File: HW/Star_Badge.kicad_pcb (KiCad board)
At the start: 2 copper layers, 180 x 171.6 mm, 55 parts, among them J1 AVR-ISP-6, J2 10118194-0001LF, Q1 Q_NMOS_DGS, Q2 Q_PMOS_DGS, U1 ATTINY861-15XD, U2 TPS613221ADBVT, U3 AP7363-33D-13, X1 Badgelife_sao_connector_v169b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, X2 Badgelife_sao_connector_v169b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, X3 Badgelife_sao_connector_v169b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

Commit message: Star 4 - net routing
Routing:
- net /EN_RGB2: track 0.00 -> 44.4 mm
- net Net-(BT1-Pad1): track 46.0 -> 48.3 mm
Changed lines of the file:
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@@
     (thickness 1.6)
     (drawings 611)
-    (tracks 85)
+    (tracks 120)
     (zones 0)
     (modules 55)
@@
   (gr_line (start 100.038258 14.223787) (end 100.038258 14.223787) (layer Edge.Cuts) (width 0.1))
   (segment (start 99.6 155.5) (end 98.95 155.5) (width 0.4572) (layer B.Cu) (net 1))
-  (segment (start 72.85 116.475) (end 66.6 124.1822) (width 0.4572) (layer B.Cu) (net 2))
   (segment (start 79.05 148.5) (end 79.2 148.65) (width 0.4572) (layer B.Cu) (net 2))
-  (segment (start 66.6 124.1822) (end 66.6 141.85) (width 0.4572) (layer B.Cu) (net 2))
-  (segment (start 66.6 141.85) (end 73.25 148.5) (width 0.4572) (layer B.Cu) (net 2))
   (segment (start 73.25 148.5) (end 79.05 148.5) (width 0.4572) (layer B.Cu) (net 2))
   (segment (start 73.2 148.55) (end 73.2 151.5) (width 0.508) (layer B.Cu) (net 2))
   (segment (start 73.25 148.5) (end 73.2 148.55) (width 0.508) (layer B.Cu) (net 2))
+  (segment (start 71.5 148.5) (end 73.25 148.5) (width 0.4572) (layer B.Cu) (net 2))
+  (segment (start 65.5 142.5) (end 71.5 148.5) (width 0.4572) (layer B.Cu) (net 2))
+  (segment (start 72.85 116.475) (end 65.5 123.825) (width 0.4572) (layer B.Cu) (net 2))
+  (segment (start 65.5 123.825) (end 65.5 142.5) (width 0.4572) (layer B.Cu) (net 2))
   (segment (start 107.4 156.45) (end 110.625 153.225) (width 0.4572) (layer B.Cu) (net 3))
   (segment (start 101.55 156) (end 102 156.45) (width 0.4572) (layer B.Cu) (net 3))
@@
   (segment (start 85.7 148.7) (end 85.7 145.6) (width 0.508) (layer B.Cu) (net 5))
   (segment (start 89 150.775) (end 89 146.625) (width 0.508) (layer B.Cu) (net 5))
+  (segment (start 80.6 128.7) (end 80.583073 128.747516) (width 0.2032) (layer B.Cu) (net 11))
+  (segment (start 77.6 125.5) (end 79.5 128.8) (width 0.2032) (layer B.Cu) (net 11))
+  (segment (start 77.3 125.3) (end 77.6 125.5) (width 0.2032) (layer B.Cu) (net 11))
+  (segment (start 73 131.4) (end 73.4 131.3) (width 0.2032) (layer B.Cu) (net 11))
+  (segment (start 72.4 131.5) (end 73 131.4) (width 0.2032) (layer B.Cu) (net 11))
+  (segment (start 76.7 125.5) (end 77 125.3) (width 0.2032) (layer B.Cu) (net 11))
+  (segment (start 73.4 131.3) (end 73.6 131.2) (width 0.2032) (layer B.Cu) (net 11))
+  (segment (start 71.518794 130.675879) (end 72.206625 131.36371) (width 0.2032) (layer B.Cu) (net 11))
+  (segment (start 79.5 128.8) (end 80.1 129.8) (width 0.2032) (layer B.Cu) (net 11))
+  (segment (start 72.206625 131.36371) (end 72.4 131.5) (width 0.2032) (layer B.Cu) (net 11))
+  (segment (start 80.1 129.8) (end 80.6 128.7) (width 0.2032) (layer B.Cu) (net 11))
+  (segment (start 76.3 126.1) (end 76.7 125.5) (width 0.2032) (layer B.Cu) (net 11))
+  (segment (start 73.6 131.2) (end 74.6 129.5) (width 0.2032) (layer B.Cu) (net 11))
+  (segment (start 74.6 129.5) (end 75.2 128.2) (width 0.2032) (layer B.Cu) (net 11))
+  (segment (start 75.2 128.2) (end 76.3 126.1) (width 0.2032) (layer B.Cu) (net 11))
+  (segment (start 77 125.3) (end 77.3 125.3) (width 0.2032) (layer B.Cu) (net 11))
+  (segment (start 80.377778 130.7) (end 80.1 129.8) (width 0.2032) (layer B.Cu) (net 11))
+  (segment (start 80.8 131.2) (end 80.377778 130.7) (width 0.2032) (layer B.Cu) (net 11))
+  (segment (start 83.7 131.8) (end 80.8 131.2) (width 0.2032) (layer B.Cu) (net 11))
+  (segment (start 87 132.3) (end 86.4 132.2) (width 0.2032) (layer B.Cu) (net 11))
+  (segment (start 87.5 133.1) (end 87.4 132.6) (width 0.2032) (layer B.Cu) (net 11))
+  (segment (start 81.1 144) (end 82.6 144.8) (width 0.2032) (layer B.Cu) (net 11))
+  (segment (start 86.4 132.2) (end 83.7 131.8) (width 0.2032) (layer B.Cu) (net 11))
+  (segment (start 82.6 144.8) (end 83.1 145.1) (width 0.2032) (layer B.Cu) (net 11))
+  (segment (start 78.7 143.55) (end 79.3 143.55) (width 0.2032) (layer B.Cu) (net 11))
+  (segment (start 82.9 138) (end 87.5 133.1) (width 0.2032) (layer B.Cu) (net 11))
+  (segment (start 87.4 132.6) (end 87 132.3) (width 0.2032) (layer B.Cu) (net 11))
+  (segment (start 79.4 143.2) (end 81.1 144) (width 0.2032) (layer B.Cu) (net 11))
+  (segment (start 83.1 145.1) (end 83.4 145) (width 0.2032) (layer B.Cu) (net 11))
+  (segment (start 83.78156 144.3) (end 83.1 139.9) (width 0.2032) (layer B.Cu) (net 11))
+  (segment (start 83.1 139.9) (end 82.9 138) (width 0.2032) (layer B.Cu) (net 11))
+  (segment (start 79.3 143.55) (end 79.4 143.2) (width 0.2032) (layer B.Cu) (net 11))
+  (segment (start 83.4 145) (end 83.625 144.683986) (width 0.2032) (layer B.Cu) (net 11))
+  (segment (start 83.625 144.683986) (end 83.78156 144.3) (width 0.2032) (layer B.Cu) (net 11))
   (segment (start 119.25 131.25) (end 117.75 131.5) (width 0.2032) (layer B.Cu) (net 12))
   (segment (start 121.5 127.186948) (end 120.78461 128.573568) (width 0.2032) (layer B.Cu) (net 12))

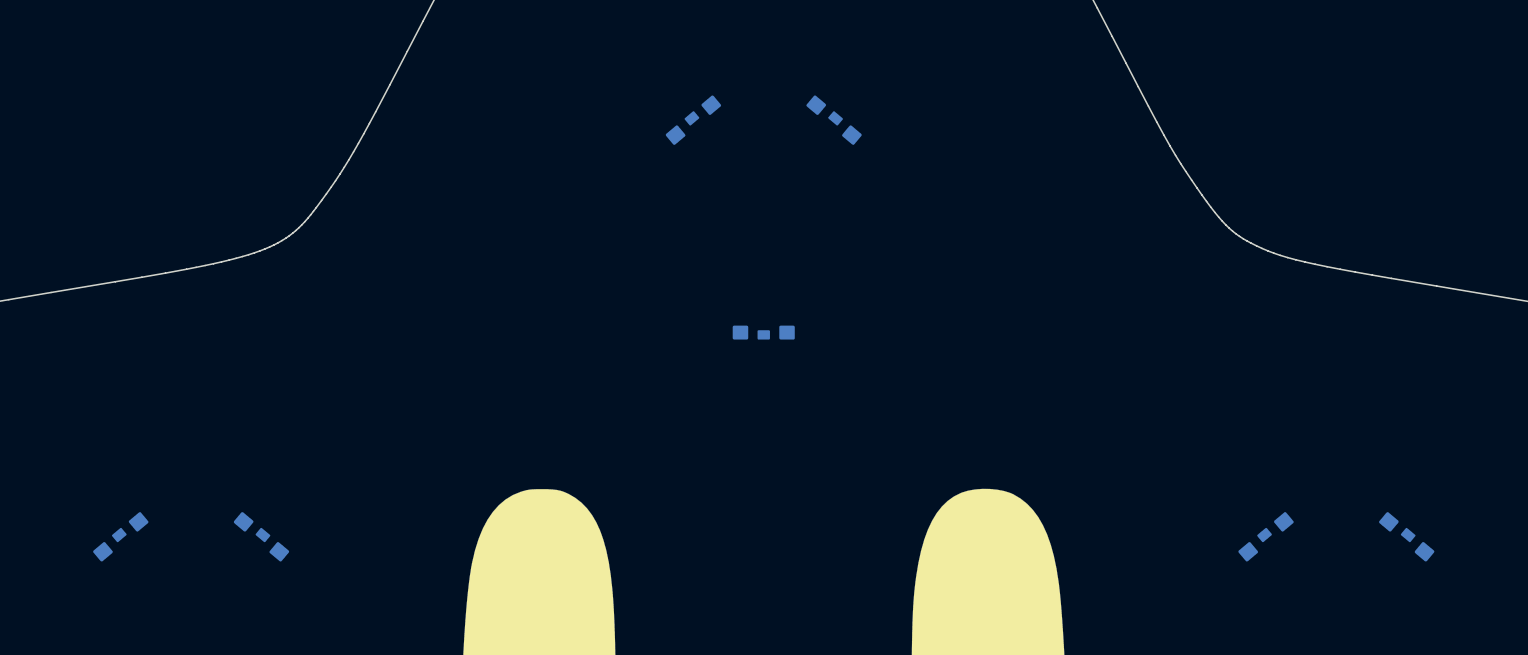
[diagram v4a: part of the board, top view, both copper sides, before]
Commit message: Adjusted the Y on the remaining LEDs
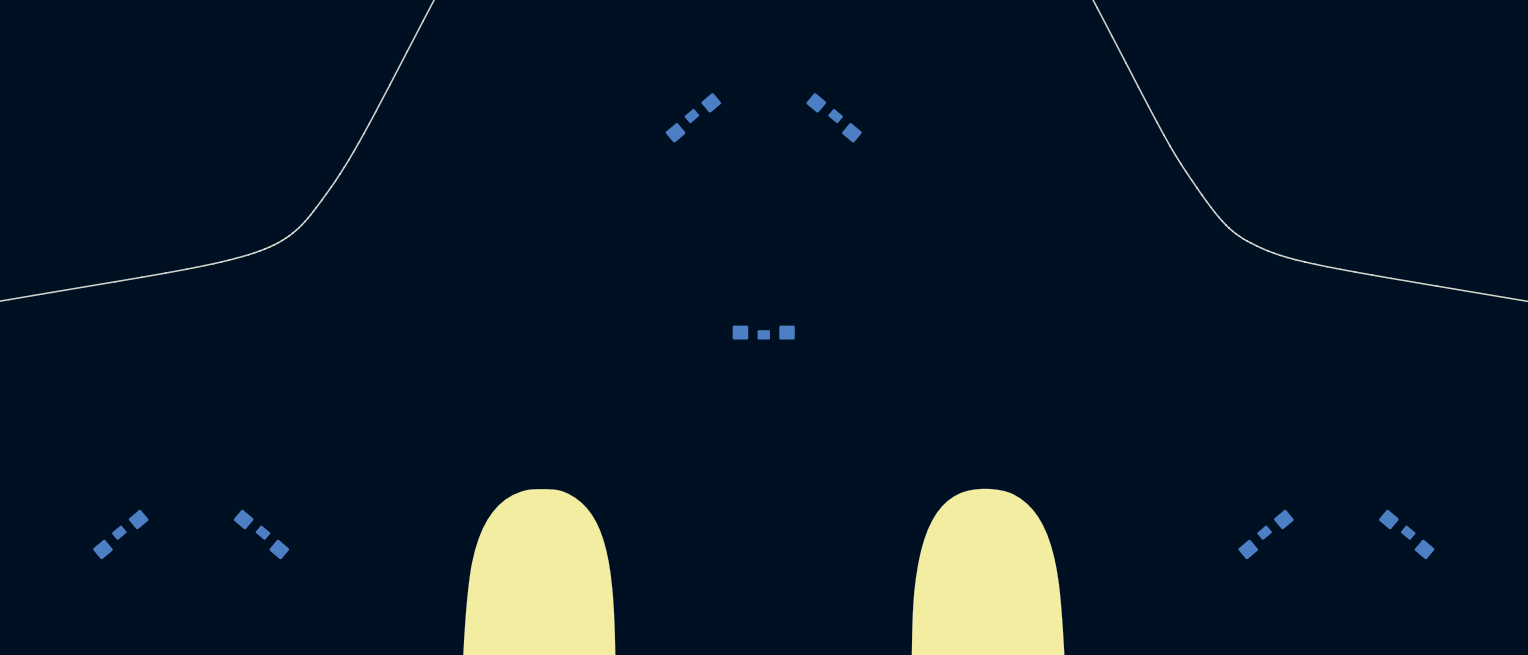
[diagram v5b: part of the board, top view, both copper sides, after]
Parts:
- moved D13 0.15 mm to (141.4, 86.3)
- moved D14 0.15 mm to (132.4, 86.3)
- moved D4 0.15 mm to (67.6, 86.3)
- moved D5 0.15 mm to (58.6, 86.3)
- moved D1 0.15 mm to (104.5, 59.5)
- moved D2 0.15 mm to (95.5, 59.5)
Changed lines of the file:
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@@
   )
   (module Star_Badge:1204_SIDE_VIEW_LED locked (layer B.Cu)
-    (at 132.4 86.5 40)
+    (at 132.4 86.35 40)
     (fp_text reference D14 (at 0.032602 -2.061295 40) (layer B.SilkS)
       (effects (font (size 0.7 0.7) (thickness 0.15)) (justify mirror))
@@
   )
   (module Star_Badge:1204_SIDE_VIEW_LED locked (layer B.Cu)
-    (at 141.4 86.5 320)
+    (at 141.4 86.35 320)
     (fp_text reference D13 (at 0.044002 -2.125574 320) (layer B.SilkS)
       (effects (font (size 0.7 0.7) (thickness 0.15)) (justify mirror))
@@
   )
   (module Star_Badge:1204_SIDE_VIEW_LED locked (layer B.Cu)
-    (at 58.6 86.5 40)
+    (at 58.6 86.35 40)
     (fp_text reference D5 (at 0.032602 -2.061295 40) (layer B.SilkS)
       (effects (font (size 0.7 0.7) (thickness 0.15)) (justify mirror))
@@
   )
   (module Star_Badge:1204_SIDE_VIEW_LED locked (layer B.Cu)
-    (at 67.6 86.5 320)
+    (at 67.6 86.35 320)
     (fp_text reference D4 (at 0.031676 -1.984691 320) (layer B.SilkS)
       (effects (font (size 0.7 0.7) (thickness 0.15)) (justify mirror))
@@
   )
   (module Star_Badge:1204_SIDE_VIEW_LED locked (layer B.Cu)
-    (at 95.5 59.65 40)
+    (at 95.5 59.5 40)
     (fp_text reference D2 (at 0 -2.12132 40) (layer B.SilkS)
       (effects (font (size 0.7 0.7) (thickness 0.15)) (justify mirror))
@@
   )
   (module Star_Badge:1204_SIDE_VIEW_LED locked (layer B.Cu)
-    (at 104.5 59.65 320)
+    (at 104.5 59.5 320)
     (fp_text reference D1 (at -0.059752 -2.208869 320) (layer B.SilkS)
       (effects (font (size 0.7 0.7) (thickness 0.15)) (justify mirror))

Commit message: Routed - net Star 5
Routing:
- net /EN_RGB1: track 0.00 -> 44.6 mm
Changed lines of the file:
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@@
     (thickness 1.6)
     (drawings 611)
-    (tracks 120)
+    (tracks 156)
     (zones 0)
     (modules 55)
@@
   (segment (start 85.7 148.7) (end 85.7 145.6) (width 0.508) (layer B.Cu) (net 5))
   (segment (start 89 150.775) (end 89 146.625) (width 0.508) (layer B.Cu) (net 5))
+  (segment (start 69.7 101.2) (end 69.7 100.9) (width 0.2032) (layer B.Cu) (net 10))
+  (segment (start 69.4 101.6) (end 69.7 101.2) (width 0.2032) (layer B.Cu) (net 10))
+  (segment (start 65 99.6) (end 66.3 100.3) (width 0.2032) (layer B.Cu) (net 10))
+  (segment (start 67.115034 100.7) (end 69.2 101.6) (width 0.2032) (layer B.Cu) (net 10))
+  (segment (start 66.3 100.3) (end 67.115034 100.7) (width 0.2032) (layer B.Cu) (net 10))
+  (segment (start 64.6 100.15) (end 65 99.6) (width 0.2032) (layer B.Cu) (net 10))
+  (segment (start 69.2 101.6) (end 69.4 101.6) (width 0.2032) (layer B.Cu) (net 10))
+  (segment (start 69.117647 97.017647) (end 69.1 96.9) (width 0.2032) (layer B.Cu) (net 10))
+  (segment (start 69.7 100.9) (end 69.117647 97.017647) (width 0.2032) (layer B.Cu) (net 10))
+  (segment (start 65.6 85.9) (end 66.483073 85.347516) (width 0.2032) (layer B.Cu) (net 10))
+  (segment (start 73.3 90) (end 73.5 89.3) (width 0.2032) (layer B.Cu) (net 10))
+  (segment (start 70.600496 92.7) (end 73.3 90) (width 0.2032) (layer B.Cu) (net 10))
+  (segment (start 69.117647 97.017647) (end 68.9 95.2) (width 0.2032) (layer B.Cu) (net 10))
+  (segment (start 68.9 95.2) (end 68.9 94.5) (width 0.2032) (layer B.Cu) (net 10))
+  (segment (start 68.9 94.5) (end 70.600496 92.7) (width 0.2032) (layer B.Cu) (net 10))
+  (segment (start 73.5 89.3) (end 72.9 88.9) (width 0.2032) (layer B.Cu) (net 10))
+  (segment (start 72.9 88.9) (end 72.5 88.8) (width 0.2032) (layer B.Cu) (net 10))
+  (segment (start 72.5 88.8) (end 71.4 88.6) (width 0.2032) (layer B.Cu) (net 10))
+  (segment (start 71.4 88.6) (end 69.4 88.3) (width 0.2032) (layer B.Cu) (net 10))
+  (segment (start 66.8 87.8) (end 65.6 85.9) (width 0.2032) (layer B.Cu) (net 10))
+  (segment (start 69.4 88.3) (end 66.8 87.8) (width 0.2032) (layer B.Cu) (net 10))
+  (segment (start 63.313366 81.9) (end 63.8 82.386634) (width 0.2032) (layer B.Cu) (net 10))
+  (segment (start 62.871294 81.9) (end 63.313366 81.9) (width 0.2032) (layer B.Cu) (net 10))
+  (segment (start 62.6 82.1) (end 62.871294 81.9) (width 0.2032) (layer B.Cu) (net 10))
+  (segment (start 59.5 87.8) (end 59.6 87.7) (width 0.2032) (layer B.Cu) (net 10))
+  (segment (start 63.8 82.389174) (end 65.6 85.9) (width 0.2032) (layer B.Cu) (net 10))
+  (segment (start 63.8 82.386634) (end 63.8 82.389174) (width 0.2032) (layer B.Cu) (net 10))
+  (segment (start 59.053924 87.96019) (end 59.5 87.8) (width 0.2032) (layer B.Cu) (net 10))
+  (segment (start 57.418794 87.275879) (end 57.9 88.1) (width 0.2032) (layer B.Cu) (net 10))
+  (segment (start 57.9 88.1) (end 59.053924 87.96019) (width 0.2032) (layer B.Cu) (net 10))
+  (segment (start 59.6 87.7) (end 60.02019 87.07981) (width 0.2032) (layer B.Cu) (net 10))
+  (segment (start 62 83.189805) (end 62.6 82.1) (width 0.2032) (layer B.Cu) (net 10))
+  (segment (start 60.02019 87.07981) (end 60.7 85.7) (width 0.2032) (layer B.Cu) (net 10))
+  (segment (start 60.7 85.7) (end 60.8 85.5) (width 0.2032) (layer B.Cu) (net 10))
+  (segment (start 60.8 85.5) (end 61.2 84.8) (width 0.2032) (layer B.Cu) (net 10))
+  (segment (start 61.2 84.8) (end 62 83.189805) (width 0.2032) (layer B.Cu) (net 10))
   (segment (start 80.6 128.7) (end 80.583073 128.747516) (width 0.2032) (layer B.Cu) (net 11))
   (segment (start 77.6 125.5) (end 79.5 128.8) (width 0.2032) (layer B.Cu) (net 11))

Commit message: Routed - net Star 1
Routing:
- net /EN_RGB0: track 0.00 -> 46.3 mm
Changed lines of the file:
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@@
     (thickness 1.6)
     (drawings 611)
-    (tracks 156)
+    (tracks 206)
     (zones 0)
     (modules 55)
@@
   (segment (start 85.7 148.7) (end 85.7 145.6) (width 0.508) (layer B.Cu) (net 5))
   (segment (start 89 150.775) (end 89 146.625) (width 0.508) (layer B.Cu) (net 5))
+  (segment (start 98.9 56.425887) (end 99.6 55.1) (width 0.2032) (layer B.Cu) (net 7))
+  (segment (start 97.4 59.3) (end 98.9 56.425887) (width 0.2032) (layer B.Cu) (net 7))
+  (segment (start 95.4 61.2) (end 95.917289 61.1) (width 0.2032) (layer B.Cu) (net 7))
+  (segment (start 95.1 61.2) (end 95.4 61.2) (width 0.2032) (layer B.Cu) (net 7))
+  (segment (start 94.708917 60.816002) (end 95.1 61.2) (width 0.2032) (layer B.Cu) (net 7))
+  (segment (start 97.8 58.532943) (end 97.4 59.3) (width 0.2032) (layer B.Cu) (net 7))
+  (segment (start 94.318794 60.425879) (end 94.708917 60.816002) (width 0.2032) (layer B.Cu) (net 7))
+  (segment (start 95.917289 61.1) (end 96.3 61) (width 0.2032) (layer B.Cu) (net 7))
+  (segment (start 96.3 61) (end 96.644795 60.655205) (width 0.2032) (layer B.Cu) (net 7))
+  (segment (start 96.644795 60.655205) (end 96.8 60.4) (width 0.2032) (layer B.Cu) (net 7))
+  (segment (start 96.8 60.4) (end 97.2 59.7) (width 0.2032) (layer B.Cu) (net 7))
+  (segment (start 97.3 59.5) (end 97.8 58.532943) (width 0.2032) (layer B.Cu) (net 7))
+  (segment (start 97.2 59.7) (end 97.3 59.5) (width 0.2032) (layer B.Cu) (net 7))
+  (segment (start 102.9 58.887639) (end 102.560859 59.239141) (width 0.2032) (layer B.Cu) (net 7))
+  (segment (start 103.3 58.4) (end 102.9 58.887639) (width 0.2032) (layer B.Cu) (net 7))
+  (segment (start 102.33153 58.835484) (end 102.560859 59.239141) (width 0.2032) (layer B.Cu) (net 7))
+  (segment (start 100.3 55.08497) (end 100.4 55.1) (width 0.2032) (layer B.Cu) (net 7))
+  (segment (start 99.6 55.08497) (end 100.3 55.08497) (width 0.2032) (layer B.Cu) (net 7))
+  (segment (start 100.4 55.1) (end 101.4 57) (width 0.2032) (layer B.Cu) (net 7))
+  (segment (start 101.4 57) (end 102 58.2) (width 0.2032) (layer B.Cu) (net 7))
+  (segment (start 102 58.2) (end 102.33153 58.835484) (width 0.2032) (layer B.Cu) (net 7))
+  (segment (start 104.2 73.9) (end 101.9 72.8) (width 0.2032) (layer B.Cu) (net 7))
+  (segment (start 105.4 74.5) (end 104.2 73.9) (width 0.2032) (layer B.Cu) (net 7))
+  (segment (start 105.9 74.8) (end 105.4 74.5) (width 0.2032) (layer B.Cu) (net 7))
+  (segment (start 105.5 61.4) (end 106.7 61.6) (width 0.2032) (layer B.Cu) (net 7))
+  (segment (start 102.64649 59.434924) (end 102.9 59.9) (width 0.2032) (layer B.Cu) (net 7))
+  (segment (start 104.085196 61.14287) (end 104.4 61.2) (width 0.2032) (layer B.Cu) (net 7))
+  (segment (start 104.4 61.2) (end 105.5 61.4) (width 0.2032) (layer B.Cu) (net 7))
+  (segment (start 102.560859 59.239141) (end 102.64649 59.434924) (width 0.2032) (layer B.Cu) (net 7))
+  (segment (start 102.9 59.9) (end 103.07575 60.227404) (width 0.2032) (layer B.Cu) (net 7))
+  (segment (start 103.5 60.9) (end 103.655936 60.97523) (width 0.2032) (layer B.Cu) (net 7))
+  (segment (start 103.07575 60.227404) (end 103.4 60.751654) (width 0.2032) (layer B.Cu) (net 7))
+  (segment (start 103.4 60.751654) (end 103.5 60.9) (width 0.2032) (layer B.Cu) (net 7))
+  (segment (start 103.655936 60.97523) (end 103.9 61.1) (width 0.2032) (layer B.Cu) (net 7))
+  (segment (start 103.9 61.1) (end 104.085196 61.14287) (width 0.2032) (layer B.Cu) (net 7))
+  (segment (start 106.5 74.6) (end 105.9 74.8) (width 0.2032) (layer B.Cu) (net 7))
+  (segment (start 110.27157 62.37157) (end 110.27157 63.033716) (width 0.2032) (layer B.Cu) (net 7))
+  (segment (start 106.7 61.6) (end 109.9 62.1) (width 0.2032) (layer B.Cu) (net 7))
+  (segment (start 109.9 62.1) (end 110.27157 62.37157) (width 0.2032) (layer B.Cu) (net 7))
+  (segment (start 109.005286 64.3) (end 108.8 64.5) (width 0.2032) (layer B.Cu) (net 7))
+  (segment (start 108.8 64.5) (end 106 67.4) (width 0.2032) (layer B.Cu) (net 7))
+  (segment (start 106 67.4) (end 105.8 67.7) (width 0.2032) (layer B.Cu) (net 7))
+  (segment (start 110.27157 63.033716) (end 109.005286 64.3) (width 0.2032) (layer B.Cu) (net 7))
+  (segment (start 105.8 67.8) (end 106 69.4) (width 0.2032) (layer B.Cu) (net 7))
+  (segment (start 105.8 67.7) (end 105.8 67.8) (width 0.2032) (layer B.Cu) (net 7))
+  (segment (start 106 69.4) (end 106.7 74.3) (width 0.2032) (layer B.Cu) (net 7))
+  (segment (start 106.7 74.3) (end 106.5 74.6) (width 0.2032) (layer B.Cu) (net 7))
+  (segment (start 101.5 73.3) (end 101.5 73.1) (width 0.2032) (layer B.Cu) (net 7))
+  (segment (start 101.8 72.8) (end 101.9 72.8) (width 0.2032) (layer B.Cu) (net 7))
+  (segment (start 101.5 73.1) (end 101.8 72.8) (width 0.2032) (layer B.Cu) (net 7))
   (segment (start 69.7 101.2) (end 69.7 100.9) (width 0.2032) (layer B.Cu) (net 10))
   (segment (start 69.4 101.6) (end 69.7 101.2) (width 0.2032) (layer B.Cu) (net 10))
